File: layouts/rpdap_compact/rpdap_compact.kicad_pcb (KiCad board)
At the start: 4 copper layers, 35.8 x 38.2 mm, 64 parts

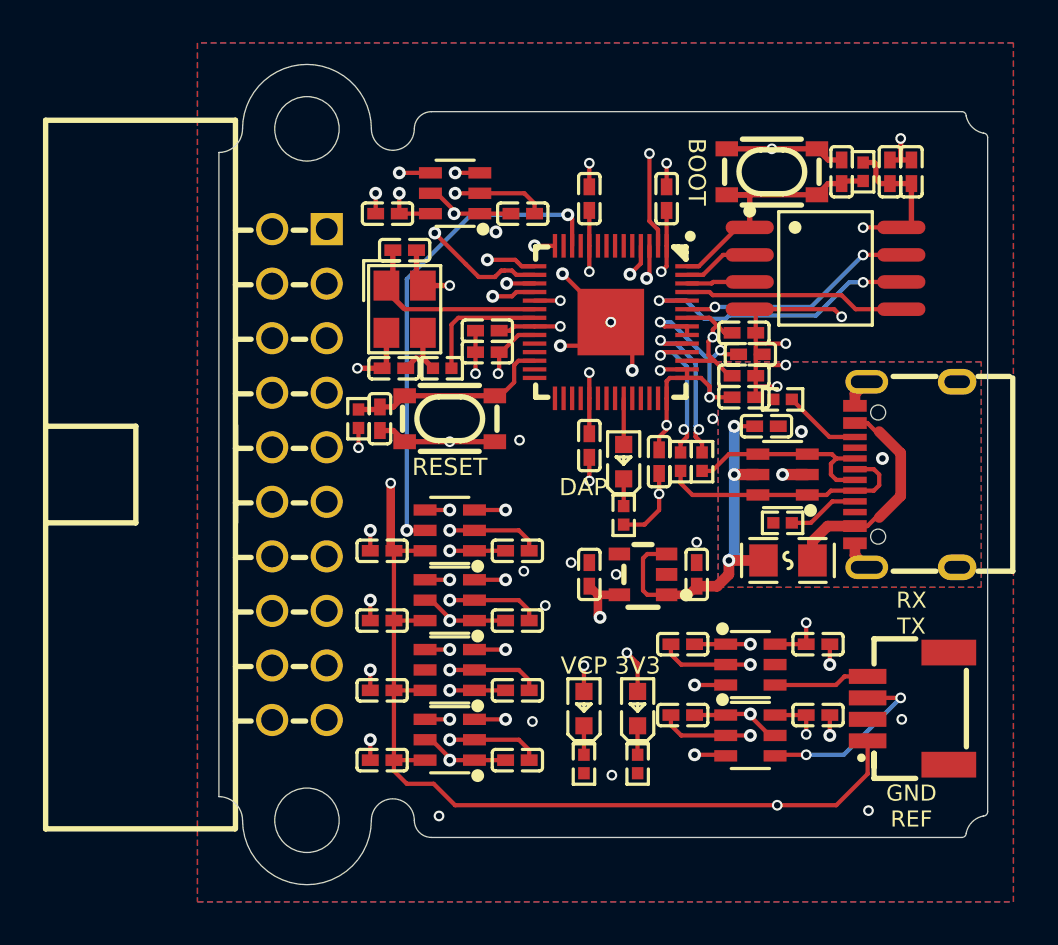
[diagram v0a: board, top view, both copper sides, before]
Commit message: fix: Update deps, swapped pinout (#2)
* rebuild with upstream rp2040 fixes. move header .25mm to the right. center dap-LED

* fix workflow triggers

* fix swapped jlink connector pinout + update deps

* pin atopile workflow version to v1.x.x
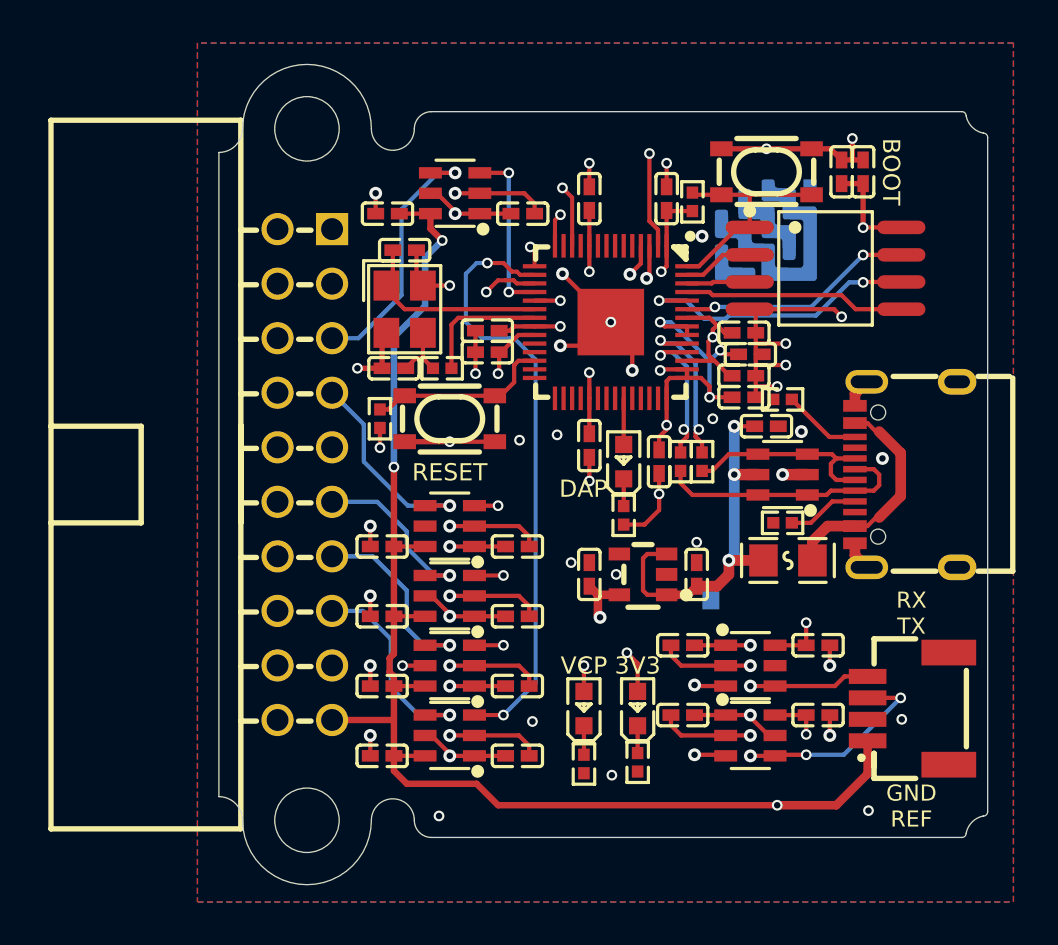
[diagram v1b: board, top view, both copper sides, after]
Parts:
- removed C15, C30: 1µF ±10% 25V X5R, Samsung_Electro_Mechanics_CL05A105KA5NQNC:C0402
- added LOGO1: , atopile_Logo_25x6mm:atopile_Logo_25x6mm, F.Cu at (25.5, -18.0)
- C16, C21, C28: value 2.2µF ±20% 6.3V X5R -> 2.2µF ±10% 16V X5R; footprint Samsung_Electro_Mechanics_CL05A225MQ5NSNC:C0402 -> Samsung_Electro_Mechanics_CL05A225KO5NQNC:C0402
- R7, R8: footprint YAGEO_RC0402FR_0727RL:R0402 -> UNI_ROYAL_0402WGF270JTCE:R0402
- X1: footprint Yangxing_Tech_X322512MSB4SI:CRYSTAL-SMD_4P-L3.2-W2.5-BL -> Abracon_LLC_ABM8_272_T3:CRYSTAL-SMD_4P-L3.2-W2.5-BL
- moved U7 28.8 mm to (24.8, -4.75), turned to -90 degrees
- moved C10 25.5 mm to (7.85, -29.0)
- moved C9 25.5 mm to (14.1, -29.0)
- moved C11 25.3 mm to (13.9, -3.80)
- moved C12 25.3 mm to (7.60, -3.80)
- moved U5 22.2 mm to (11.0, -30.0)
- moved U1 14.0 mm to (10.8, -8.00), turned to 90 degrees
- moved R3 8.07 mm to (22.1, -29.6)
- moved C8 6.70 mm to (7.60, -13.5)
- moved C7 6.70 mm to (13.9, -13.5)
- moved C3 6.30 mm to (13.9, -7.05)
- moved C4 6.30 mm to (7.60, -7.05)
- moved U4 3.45 mm to (10.8, -14.5)
- moved U8 3.25 mm to (24.8, -8.00)
- moved U3 3.05 mm to (10.8, -11.2)
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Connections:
- net A renamed input-A
- net RP_USB_N renamed output-USB_D_N
- net RP_USB_P renamed output-USB_D_P
- net USB_N renamed input-USB_D_N
- net USB_P renamed input-USB_D_P
- C1 pad 1: _power_vbus-VCC -> Vbus_fused
- C31 pad 1: _power_vbus-VCC -> Vbus_fused
- CN1 pad 3: uart-TX -> uart_connector-uart-TX
- CN1 pad 4: uart-RX -> uart_connector-uart-RX
- D1 pad 5: _power_vbus-VCC -> Vbus_fused
- F1 pad 2: _power_vbus-VCC -> Vbus_fused
- J1 pad 1: reference-VCC -> Vbus_fused
- J1 pad 11: return_test_clock-line -> TCK_SWCLK
- J1 pad 13: TDO_SWO -> TMS_DIO
- J1 pad 14: _14 -> GND
- J1 pad 15: nRESET -> TDI
- J1 pad 16: _16 -> GND
- J1 pad 17: DBGRQ -> N_TRST
- J1 pad 18: _18 -> GND
- J1 pad 19: _power_vbus-VCC -> reference-VCC
- J1 pad 3: N_TRST -> DBGRQ
- J1 pad 4: GND -> _4
- J1 pad 5: TDI -> nRESET
- J1 pad 6: GND -> _6
- J1 pad 7: TMS_DIO -> TDO_SWO
- J1 pad 8: GND -> _8
- J1 pad 9: TCK_SWCLK -> _9
- R3 pad 1: 3V3 -> chip_select
- R3 pad 2: chip_select -> 3V3
- R6 pad 1: 3V3 -> RUN
- R6 pad 2: RUN -> 3V3
- SW1 pad 1: GND -> chip_select
- SW1 pad 2: GND -> chip_select
- SW1 pad 3: chip_select -> GND
- SW1 pad 4: chip_select -> GND
- SW2 pad 1: GND -> RUN
- SW2 pad 2: GND -> RUN
- SW2 pad 3: RUN -> GND
- SW2 pad 4: RUN -> GND
- U1 pad 3: a-RX -> gpio[12]-A
- U1 pad 4: uart-RX -> TMS_DIO
- U1 pad 5: GND -> DIR
- U2 pad 1: _power_vbus-VCC -> Vbus_fused
- U2 pad 3: _power_vbus-VCC -> Vbus_fused
- U3 pad 3: model-a-line-0 -> gpio[11]-A
- U3 pad 4: TMS_DIO -> TCK_SWCLK
- U3 pad 5: dir-line -> 3V3
- U4 pad 3: model-a-line-1 -> gpio[14]-A
- U4 pad 4: TCK_SWCLK -> TDO_SWO
- U4 pad 5: 3V3 -> GND
- U5 pad 3: model-a-line-2 -> gpio[15]-A
- U5 pad 4: TDO_SWO -> nRESET
- U5 pad 5: GND -> 3V3
- U6 pad 3: model-a-line-3 -> gpio[13]-A
- U6 pad 4: nRESET -> TDI
- U7 pad 3: model-a-line-4 -> mcu-uart-TX
- U7 pad 4: TDI -> uart_connector-uart-TX
- U8 pad 3: a-TX -> mcu-uart-RX
- U8 pad 4: uart-TX -> uart_connector-uart-RX
- U8 pad 5: 3V3 -> GND
- U9 pad 12: dir-line -> DIR
- U9 pad 14: model-a-line-1 -> gpio[11]-A
- U9 pad 15: model-a-line-0 -> gpio[12]-A
- U9 pad 16: model-a-line-4 -> gpio[13]-A
- U9 pad 17: model-a-line-2 -> gpio[14]-A
- U9 pad 18: model-a-line-3 -> gpio[15]-A
- U9 pad 2: a-TX -> mcu-uart-TX
- U9 pad 3: a-RX -> mcu-uart-RX
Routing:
- net Vbus_fused: track 0.00 -> 47.9 mm, vias 0 -> 3
- net _power_vbus-VCC: track 43.8 -> 0.00 mm, vias 3 -> 0
- net mcu-uart-TX: track 0.00 -> 37.9 mm, vias 0 -> 2
- net a-TX: track 37.9 -> 0.00 mm, vias 2 -> 0
- net DIR: track 0.00 -> 34.5 mm, vias 0 -> 2
- net gpio[13]-A: track 0.00 -> 28.4 mm, vias 0 -> 2
- net model-a-line-3: track 26.1 -> 0.00 mm, vias 2 -> 0
- net model-a-line-1: track 23.6 -> 0.00 mm, vias 2 -> 0
- net mcu-uart-RX: track 0.00 -> 22.9 mm, vias 0 -> 2
- net a-RX: track 22.9 -> 0.00 mm, vias 2 -> 0
- net dir-line: track 22.8 -> 0.00 mm, vias 2 -> 0
- net gpio[12]-A: track 0.00 -> 22.5 mm, vias 0 -> 2
- net model-a-line-2: track 22.3 -> 0.00 mm, vias 2 -> 0
- net gpio[11]-A: track 0.00 -> 20.8 mm, vias 0 -> 2
- net model-a-line-0: track 17.2 -> 0.00 mm, vias 2 -> 0
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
